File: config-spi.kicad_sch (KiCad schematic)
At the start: 39 parts, among them J3 PinHeader_2x7_P2mm_Drill1mm_S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, Q1 BSS138PW, Q2 BSS138PW, U7 S25FL128SAGNFI000, U8 XC7K160T-FFG676

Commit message: [#80386] Update Manufacturer of FPGA chip
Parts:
- U8: Manufacturer Xilinx -> AMD-Xilinx
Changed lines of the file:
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@@
 			)
 		)
-		(property "Description" ""
+		(property "Description" "FPGA Kintex-7 Family 162240 Cells 28nm Technology"
 			(at 290.195 89.535 0)
 			(effects
@@
 			)
 		)
-		(property "Manufacturer" "Xilinx"
+		(property "Manufacturer" "AMD-Xilinx"
 			(at 290.195 89.535 0)
 			(effects

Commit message: [#80386] Add company name in board settings
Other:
- company: Antmicro Ltd. -> Antmicro
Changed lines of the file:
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@@
 		(date "2023-07-27")
 		(rev "1.0.1")
-		(company "Antmicro Ltd.")
+		(company "Antmicro")
 		(comment 1 "www.antmicro.com")
-		(comment 2 "Antmicro Ltd")
 	)
 	(text "Master SPI Quad (x4) configuration scheme"

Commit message: [#87036] Update components, clear DRC and ERC
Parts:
- removed D4: TPD6E05U06RVZR, data-center-rdimm-ddr5-tester-footprints:USON-14_3.5X1.3X0.5mm_P0.5mm, symbol data-center-rdimm-ddr5-tester:TPD6E05U06RVZR
- added D4: TPD6E05U06RVZR, antmicro-footprints:USON-14_3.5X1.3X0.5mm_P0.5mm, symbol antmicroTVSDiodes:TPD6E05U06RVZR
- C43: footprint data-center-rdimm-ddr5-tester-footprints:C_0402_1005Metric -> antmicro-footprints:C_0402_1005Metric; symbol data-center-rdimm-ddr5-tester:C_100n_6V3_0402 -> antmicroCapacitorsmisc:C_100n_6V3_0402; Public (none) -> False
- C44: footprint data-center-rdimm-ddr5-tester-footprints:C_0603_1608Metric -> antmicro-footprints:C_0603_1608Metric; symbol data-center-rdimm-ddr5-tester:C_47u_0603 -> antmicroCapacitors0603:C_47u_0603
- C45, C46: footprint data-center-rdimm-ddr5-tester-footprints:C_0402_1005Metric -> antmicro-footprints:C_0402_1005Metric; symbol data-center-rdimm-ddr5-tester:C_470n_0402 -> antmicroCapacitors0402:C_470n_0402
- D5, D6: footprint data-center-rdimm-ddr5-tester-footprints:LED_0603_1608Metric_G -> antmicro-footprints:LED_0603_1608Metric_G; symbol data-center-rdimm-ddr5-tester:LED_G_0603_KP-1608CGCK -> antmicroLEDIndicationDiscrete:LED_G_0603_KP-1608CGCK; Color (none) -> Green
- EMCCLK1, PUDC_B1: footprint data-center-rdimm-ddr5-tester-footprints:Testpoint_smd_1mm -> antmicro-footprints:TP_SMD_1mm; symbol data-center-rdimm-ddr5-tester:TP_1mm_SMD -> antmicroTestPoints:TP_1mm_SMD
- MODE1: footprint data-center-rdimm-ddr5-tester-footprints:PinHeader_1x3_P2.54_Drill1.1mm -> antmicro-footprints:PinHeader_1x3_P2.54mm_Drill1.1mm; symbol data-center-rdimm-ddr5-tester:PinHeader_1x3_P2.54mm_Drill1.1mm -> antmicroGenericPinHeaders:PinHeader_1x3_P2.54mm_Drill1.1mm
- PROG_B1: footprint data-center-rdimm-ddr5-tester-footprints:SW_B3U-3000P -> antmicro-footprints:SW_B3U-1000P_SMD; symbol data-center-rdimm-ddr5-tester:SW_B3U-1000P -> antmicroPushbuttonSwitches:SW_B3U-1000P_SMD; Manufacturer Omron Electronics -> Omron
- Q1, Q2: footprint data-center-rdimm-ddr5-tester-footprints:SC70-3 -> antmicro-footprints:SC70-3; symbol data-center-rdimm-ddr5-tester:BSS138PW -> antmicroTransistorsFETsMOSFETsSingle:BSS138PW
- R35, R36, R37, R38, R39, R40, R48, R51, R55: footprint data-center-rdimm-ddr5-tester-footprints:R_0402_1005Metric -> antmicro-footprints:R_0402_1005Metric; symbol data-center-rdimm-ddr5-tester:R_0R_0402 -> antmicroResistors0402:R_0R_0402
- R41: footprint data-center-rdimm-ddr5-tester-footprints:R_0402_1005Metric -> antmicro-footprints:R_0402_1005Metric; symbol data-center-rdimm-ddr5-tester:R_2k2_0402 -> antmicroResistors0402:R_2k2_0402
- R42, R43, R57: footprint data-center-rdimm-ddr5-tester-footprints:R_0402_1005Metric -> antmicro-footprints:R_0402_1005Metric; symbol data-center-rdimm-ddr5-tester:R_100R_0402 -> antmicroResistors0402:R_100R_0402; DNP DNP -> (none); now not fitted; now left out of the parts list
- R44, R45, R52, R53: footprint data-center-rdimm-ddr5-tester-footprints:R_0402_1005Metric -> antmicro-footprints:R_0402_1005Metric; symbol data-center-rdimm-ddr5-tester:R_4k7_0402 -> antmicroResistors0402:R_4k7_0402
- R46, R47, R54: footprint data-center-rdimm-ddr5-tester-footprints:R_0402_1005Metric -> antmicro-footprints:R_0402_1005Metric; symbol data-center-rdimm-ddr5-tester:R_330R_0402 -> antmicroResistors0402:R_330R_0402
- R49, R50: footprint data-center-rdimm-ddr5-tester-footprints:R_0402_1005Metric -> antmicro-footprints:R_0402_1005Metric; symbol data-center-rdimm-ddr5-tester:R_0R_0402 -> antmicroResistors0402:R_0R_0402; DNP DNP -> (none); now not fitted; now left out of the parts list
- R56: footprint data-center-rdimm-ddr5-tester-footprints:R_0402_1005Metric -> antmicro-footprints:R_0402_1005Metric; symbol data-center-rdimm-ddr5-tester:R_100R_0402 -> antmicroResistors0402:R_100R_0402
- U7: footprint data-center-rdimm-ddr5-tester-footprints:WSON-8_6x8x0.5mm_P1.27mm -> antmicro-footprints:WSON-8_6x8x0.5mm_P1.27mm; symbol data-center-rdimm-ddr5-tester:S25FL128SAGNFI000 -> antmicroMemory:S25FL128SAGNFI000
- U8: footprint data-center-rdimm-ddr5-tester-footprints:BGA-676_27x27mm_Layout26x26_P1X1mm -> antmicro-footprints:BGA-676_27x27mm_Layout26x26_P1x1mm_FFG676; symbol data-center-rdimm-ddr5-tester:XC7K160T-FFG676 -> antmicroFPGAChips:XC7K160T-FFG676
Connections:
- net GND: now also D4.10 (GND), D4.5 (GND); no longer U7.9 (EP)
- net TCK_JTAG: now also D4.13 (D1-), D4.2 (D1-)
- net TDI_JTAG: now also D4.7 (D3-), D4.8 (D3-)
- net TDO_JTAG: now also D4.6 (D3+), D4.9 (D3+)
- net TMS_JTAG: now also D4.1 (D1+), D4.14 (D1+)
- net at R46.1: now also D5.1 (C); no longer D5.2
- net at R47.1: now also D6.1 (C); no longer D6.2
- net 3V3_SYS renamed +3V3
- net +3V3: now also D5.2 (A), D6.2 (A); no longer D5.1, D6.1
- new net: D4.11 (D2-), D4.4 (D2-)
- new net: D4.12 (D2+), D4.3 (D2+)
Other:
- moved on the sheet: C43, C45, C46, D5, D6, J3, MODE1, R35, R45, R48, R51, R52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

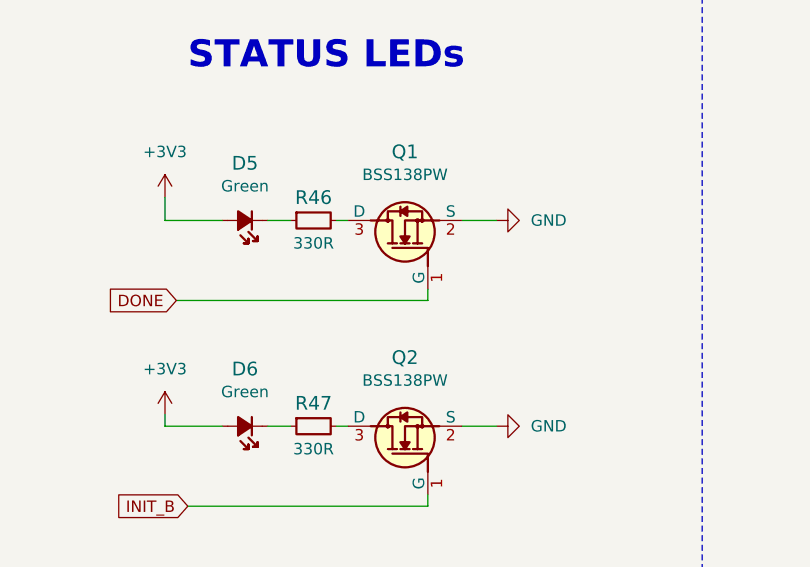
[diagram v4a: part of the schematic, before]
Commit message: [#87036] Update BSS138 transistors
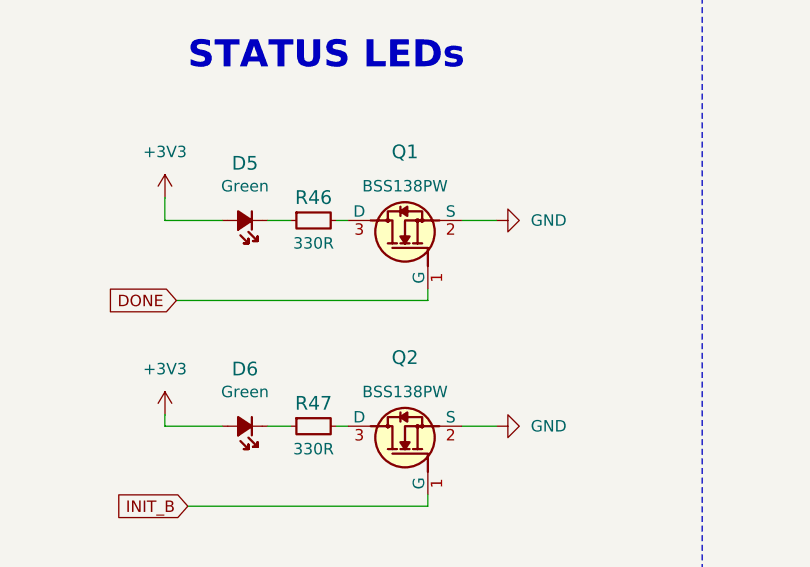
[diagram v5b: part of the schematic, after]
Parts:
- Q1, Q2: symbol antmicroTransistorsFETsMOSFETsSingle:BSS138PW -> antmicroTransistorsFETsMOSFETsSingle:BSS138PW,115; MPN BSS138PW -> BSS138PW,115
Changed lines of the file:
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@@
 	)
 	(symbol
-		(lib_id "antmicroTransistorsFETsMOSFETsSingle:BSS138PW")
+		(lib_id "antmicroTransistorsFETsMOSFETsSingle:BSS138PW,115")
 		(at 165.1 234.95 90)
 		(unit 1)
@@
 		)
 		(property "Value" "BSS138PW"
-			(at 162.56 222.25 90)
+			(at 162.56 223.52 90)
 			(effects
 				(font
@@
 		)
 		(property "Description" "Power MOSFET, N Channel, 60 V, 320 mA, 0.9 ohm, SOT-323, Surface Mount"
-			(at 165.1 234.95 0)
+			(at 191.77 212.09 0)
 			(effects
 				(font
 					(size 1.27 1.27)
 				)
+				(justify left bottom)
 				(hide yes)
 			)
 		)
-		(property "MPN" "BSS138PW"
-			(at 181.61 212.09 0)
+		(property "MPN" "BSS138PW,115"
+			(at 162.56 223.52 90)
 			(effects
 				(font
@@
 					(thickness 0.15)
 				)
-				(justify left bottom)
 				(hide yes)
 			)
@@
 	)
 	(symbol
-		(lib_id "antmicroTransistorsFETsMOSFETsSingle:BSS138PW")
+		(lib_id "antmicroTransistorsFETsMOSFETsSingle:BSS138PW,115")
 		(at 165.1 257.81 90)
 		(unit 1)
@@
 		)
 		(property "Value" "BSS138PW"
-			(at 162.56 245.11 90)
+			(at 162.56 246.38 90)
 			(effects
 				(font
@@
 		)
 		(property "Description" "Power MOSFET, N Channel, 60 V, 320 mA, 0.9 ohm, SOT-323, Surface Mount"
-			(at 165.1 257.81 0)
+			(at 191.77 234.95 0)
 			(effects
 				(font
 					(size 1.27 1.27)
 				)
+				(justify left bottom)
 				(hide yes)
 			)
 		)
-		(property "MPN" "BSS138PW"
-			(at 181.61 234.95 0)
+		(property "MPN" "BSS138PW,115"
+			(at 162.56 246.38 90)
 			(effects
 				(font
@@
 					(thickness 0.15)
 				)
-				(justify left bottom)
 				(hide yes)
 			)
